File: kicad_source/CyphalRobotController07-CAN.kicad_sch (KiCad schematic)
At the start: 32 parts, among them J1 BM04B-SRSS-TB, J15 PinHeader_1x04, J16 PinHeader_1x04, J17 PinHeader_1x05, J2 RASPBERRYPI_PICO, J3 BM04B-SRSS-TB, J4 B3B-PH-SM4-TB, SW1 PTS636 SM43 SMTR LFS, U1 24LC64-I/SN, U17 SN74LVC2T45DCUR, U18 SN74LVC2T45DCUR

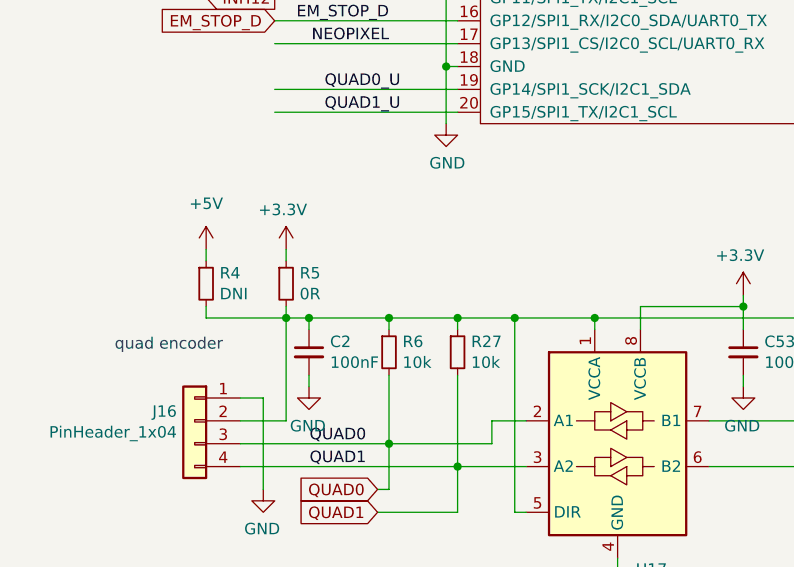
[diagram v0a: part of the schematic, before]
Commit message: finished layout near encoder level converter
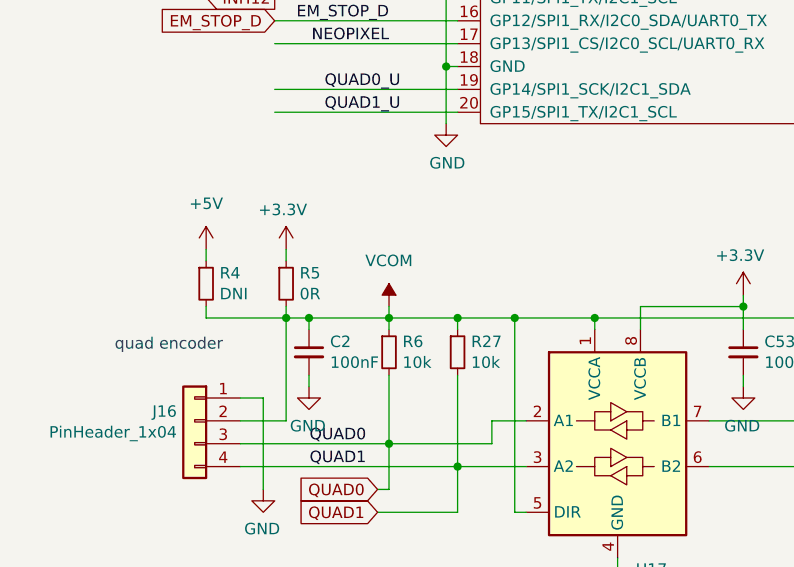
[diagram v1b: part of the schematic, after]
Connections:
- net VCOM: now reaches C2.1, C54.1, J15.2 (Pin_2), J16.2 (Pin_2), R27.1, R4.2, R5.2, R57.1, R58.1, R6.1, U17.1 (VCCA), U17.5 (DIR), U18.1 (VCCA), U18.5 (DIR)
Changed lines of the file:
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@@
+    (stroke (width 0) (type default) (color 0 0 0 0))
+  )
+  (wire (pts (xy 53.34 90.17) (xy 53.34 91.44))
     (stroke (width 0) (type default) (color 0 0 0 0))
   )
@@
     (pin "5")
   )
+  (symbol (lib_id "power:VCOM") (at 53.34 90.17 0) (unit 1)
+    (in_bom yes) (on_board yes) (fields_autoplaced)
+    (property "Reference" "#PWR?" (id 0) (at 53.34 93.98 0)
+      (effects (font (size 1.27 1.27)) hide)
+    )
+    (property "Value" "VCOM" (id 1) (at 53.34 85.09 0))
+    (property "Footprint" "" (id 2) (at 53.34 90.17 0)
+      (effects (font (size 1.27 1.27)) hide)
+    )
+    (property "Datasheet" "" (id 3) (at 53.34 90.17 0)
+      (effects (font (size 1.27 1.27)) hide)
+    )
+    (pin "1")
+  )
   (symbol (lib_id "Connector_Generic_MountingPin:Conn_01x03_MountingPin") (at 157.48 148.59 0) (mirror y) (unit 1)
     (in_bom yes) (on_board yes) (fields_autoplaced)
@@
       (reference "#PWR043") (unit 1) (value "GND") (footprint "")
     )
-    (path "/29c3546c-5738-4410-83a1-968e85712add/5bfbf133-5ed7-46d0-b93e-5a5eeb84dcff"
-      (reference "#PWR044") (unit 1) (value "+3.3V") (footprint "")
-    )
     (path "/29c3546c-5738-4410-83a1-968e85712add/09e143e1-e556-491f-aa8e-93db6198adbc"
       (reference "#PWR045") (unit 1) (value "GND") (footprint "")
@@
       (reference "#PWR047") (unit 1) (value "GND") (footprint "")
     )
-    (path "/29c3546c-5738-4410-83a1-968e85712add/900bbe2d-04d2-4af8-9360-ab393613f74d"
-      (reference "#PWR048") (unit 1) (value "+3.3V") (footprint "")
-    )
     (path "/29c3546c-5738-4410-83a1-968e85712add/00000000-0000-0000-0000-00005df4db84"
       (reference "#PWR049") (unit 1) (value "GND") (footprint "")
@@
       (reference "#PWR0171") (unit 1) (value "GND") (footprint "")
     )
+    (path "/29c3546c-5738-4410-83a1-968e85712add/34b66a16-dee4-4c29-bdba-a98382440c94"
+      (reference "#PWR?") (unit 1) (value "VCOM") (footprint "")
+    )
+    (path "/4eb5a8e0-4e6e-4b4e-8de1-2650692615d2"
+      (reference "#PWR?") (unit 1) (value "VCOM") (footprint "")
+    )
+    (path "/29c3546c-5738-4410-83a1-968e85712add/60f26f94-1bb8-4efc-8f30-f83cde330d36"
+      (reference "#PWR?") (unit 1) (value "VCOM") (footprint "")
+    )
     (path "/00000000-0000-0000-0000-000062524b56"

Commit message: used raspberry pi pico with headers
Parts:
- J2: footprint generationmake:RASPI_PICO_SOLDER_Kopie -> generationmake:RASPI_PICO_SOLDER_NO_MOUNTING
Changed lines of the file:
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@@
   (title_block
     (title "CyphalRobotController07/CAN")
-    (date "2024-01-04")
+    (date "2024-01-21")
     (rev "0.2")
     (company "generationmake")
@@
     (property "Reference" "J2" (id 0) (at 100.33 14.605 0))
     (property "Value" "RASPBERRYPI_PICO" (id 1) (at 100.33 16.9164 0))
-    (property "Footprint" "generationmake:RASPI_PICO_SOLDER_Kopie" (id 2) (at 100.33 44.45 0)
+    (property "Footprint" "generationmake:RASPI_PICO_SOLDER_NO_MOUNTING" (id 2) (at 100.33 44.45 0)
       (effects (font (size 1.27 1.27)) hide)
     )
@@
   (symbol (lib_id "power:VCOM") (at 53.34 90.17 0) (unit 1)
     (in_bom yes) (on_board yes) (fields_autoplaced)
-    (property "Reference" "#PWR?" (id 0) (at 53.34 93.98 0)
+    (property "Reference" "#PWR0172" (id 0) (at 53.34 93.98 0)
       (effects (font (size 1.27 1.27)) hide)
     )
@@
       (reference "#PWR0171") (unit 1) (value "GND") (footprint "")
     )
+    (path "/4eb5a8e0-4e6e-4b4e-8de1-2650692615d2"
+      (reference "#PWR0172") (unit 1) (value "VCOM") (footprint "")
+    )
     (path "/29c3546c-5738-4410-83a1-968e85712add/34b66a16-dee4-4c29-bdba-a98382440c94"
-      (reference "#PWR?") (unit 1) (value "VCOM") (footprint "")
-    )
-    (path "/4eb5a8e0-4e6e-4b4e-8de1-2650692615d2"
-      (reference "#PWR?") (unit 1) (value "VCOM") (footprint "")
+      (reference "#PWR0173") (unit 1) (value "VCOM") (footprint "")
     )
     (path "/29c3546c-5738-4410-83a1-968e85712add/60f26f94-1bb8-4efc-8f30-f83cde330d36"
-      (reference "#PWR?") (unit 1) (value "VCOM") (footprint "")
+      (reference "#PWR0174") (unit 1) (value "VCOM") (footprint "")
     )
     (path "/00000000-0000-0000-0000-000062524b56"
@@
     )
     (path "/00000000-0000-0000-0000-0000629e332f"
-      (reference "J2") (unit 1) (value "RASPBERRYPI_PICO") (footprint "generationmake:RASPI_PICO_SOLDER_Kopie")
+      (reference "J2") (unit 1) (value "RASPBERRYPI_PICO") (footprint "generationmake:RASPI_PICO_SOLDER_NO_MOUNTING")
     )
     (path "/00000000-0000-0000-0000-00006250779d"

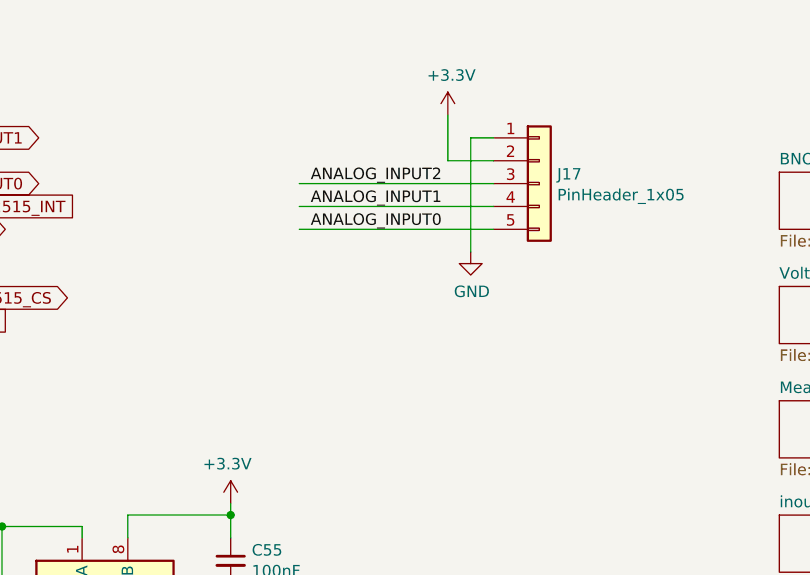
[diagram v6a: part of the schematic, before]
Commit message: connected current sense output to analog in of RP2040
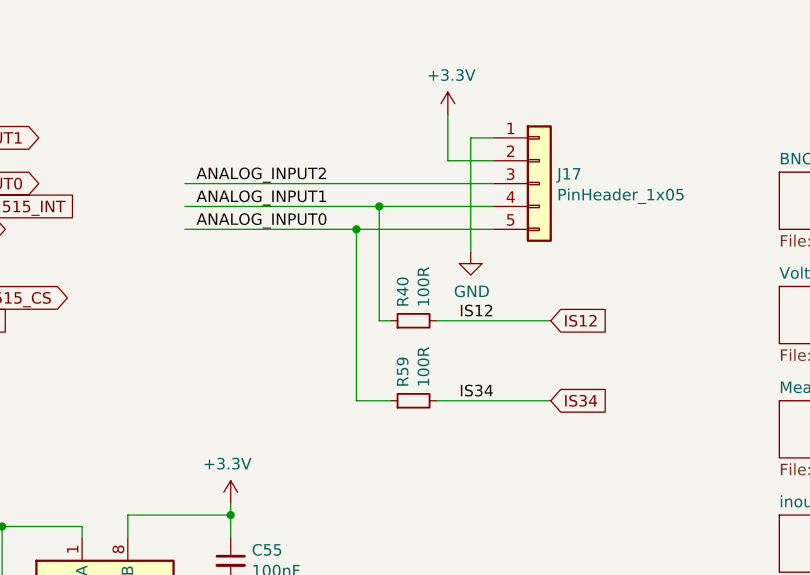
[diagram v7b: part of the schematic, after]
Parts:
- added R40, R59: 100R, Resistor_SMD:R_0603_1608Metric, symbol Device:R_Small
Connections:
- net ANALOG_INPUT0: now also R59.1
- net ANALOG_INPUT1: now also R40.1
- new net IS12: R40.2
- new net IS34: R59.2
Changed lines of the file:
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@@
   (junction (at 67.31 91.44) (diameter 0) (color 0 0 0 0)
   )
+  (junction (at 209.55 55.88) (diameter 0) (color 0 0 0 0)
+  )
   (junction (at 30.48 142.24) (diameter 0) (color 0 0 0 0)
   )
@@
   )
   (junction (at 44.45 91.44) (diameter 0) (color 0 0 0 0)
+  )
+  (junction (at 207.01 58.42) (diameter 0) (color 0 0 0 0)
   )
   (junction (at 49.53 154.94) (diameter 0) (color 0 0 0 0)
@@
     (stroke (width 0) (type default) (color 0 0 0 0))
   )
+  (wire (pts (xy 215.9 77.47) (xy 228.6 77.47))
+    (stroke (width 0) (type default) (color 0 0 0 0))
+  )
   (wire (pts (xy 114.3 148.59) (xy 111.76 148.59))
     (stroke (width 0) (type default) (color 0 0 0 0))
@@
     (stroke (width 0) (type default) (color 0 0 0 0))
   )
+  (wire (pts (xy 207.01 58.42) (xy 207.01 77.47))
+    (stroke (width 0) (type default) (color 0 0 0 0))
+  )
   (wire (pts (xy 165.1 40.64) (xy 139.7 40.64))
     (stroke (width 0) (type default) (color 0 0 0 0))
@@
     (stroke (width 0) (type default) (color 0 0 0 0))
   )
+  (wire (pts (xy 207.01 58.42) (xy 222.25 58.42))
+    (stroke (width 0) (type default) (color 0 0 0 0))
+  )
   (wire (pts (xy 168.91 148.59) (xy 168.91 144.78))
     (stroke (width 0) (type default) (color 0 0 0 0))
@@
     (stroke (width 0) (type default) (color 0 0 0 0))
   )
-  (wire (pts (xy 200.66 53.34) (xy 222.25 53.34))
-    (stroke (width 0) (type default) (color 0 0 0 0))
-  )
   (wire (pts (xy 137.16 105.41) (xy 153.67 105.41))
     (stroke (width 0) (type default) (color 0 0 0 0))
@@
     (stroke (width 0) (type default) (color 0 0 0 0))
   )
+  (wire (pts (xy 209.55 55.88) (xy 222.25 55.88))
+    (stroke (width 0) (type default) (color 0 0 0 0))
+  )
   (wire (pts (xy 165.1 105.41) (xy 165.1 102.87))
     (stroke (width 0) (type default) (color 0 0 0 0))
@@
     (stroke (width 0) (type default) (color 0 0 0 0))
   )
+  (wire (pts (xy 209.55 55.88) (xy 209.55 68.58))
+    (stroke (width 0) (type default) (color 0 0 0 0))
+  )
   (wire (pts (xy 137.16 107.95) (xy 161.29 107.95))
     (stroke (width 0) (type default) (color 0 0 0 0))
   )
-  (wire (pts (xy 200.66 58.42) (xy 222.25 58.42))
+  (wire (pts (xy 187.96 58.42) (xy 207.01 58.42))
     (stroke (width 0) (type default) (color 0 0 0 0))
   )
@@
     (stroke (width 0) (type default) (color 0 0 0 0))
   )
+  (wire (pts (xy 210.82 77.47) (xy 207.01 77.47))
+    (stroke (width 0) (type default) (color 0 0 0 0))
+  )
   (wire (pts (xy 162.56 148.59) (xy 168.91 148.59))
     (stroke (width 0) (type default) (color 0 0 0 0))
   )
-  (wire (pts (xy 200.66 55.88) (xy 222.25 55.88))
+  (wire (pts (xy 187.96 55.88) (xy 209.55 55.88))
     (stroke (width 0) (type default) (color 0 0 0 0))
   )
@@
     (stroke (width 0) (type default) (color 0 0 0 0))
   )
+  (wire (pts (xy 210.82 68.58) (xy 209.55 68.58))
+    (stroke (width 0) (type default) (color 0 0 0 0))
+  )
   (wire (pts (xy 165.1 35.56) (xy 139.7 35.56))
+    (stroke (width 0) (type default) (color 0 0 0 0))
+  )
+  (wire (pts (xy 215.9 68.58) (xy 228.6 68.58))
+    (stroke (width 0) (type default) (color 0 0 0 0))
+  )
+  (wire (pts (xy 187.96 53.34) (xy 222.25 53.34))
     (stroke (width 0) (type default) (color 0 0 0 0))
   )
@@
     (effects (font (size 1.27 1.27)) (justify right bottom))
   )
+  (label "IS12" (at 218.44 68.58 0)
+    (effects (font (size 1.27 1.27)) (justify left bottom))
+  )
   (label "MP2" (at 55.88 184.15 0)
     (effects (font (size 1.27 1.27)) (justify left bottom))
@@
     (effects (font (size 1.27 1.27)) (justify right bottom))
   )
-  (label "ANALOG_INPUT2" (at 201.93 53.34 0)
+  (label "IS34" (at 218.44 77.47 0)
+    (effects (font (size 1.27 1.27)) (justify left bottom))
+  )
+  (label "ANALOG_INPUT2" (at 189.23 53.34 0)
     (effects (font (size 1.27 1.27)) (justify left bottom))
   )
@@
     (effects (font (size 1.27 1.27)) (justify right bottom))
   )
-  (label "ANALOG_INPUT0" (at 201.93 58.42 0)
+  (label "ANALOG_INPUT0" (at 189.23 58.42 0)
     (effects (font (size 1.27 1.27)) (justify left bottom))
   )
@@
     (effects (font (size 1.27 1.27)) (justify right bottom))
   )
-  (label "ANALOG_INPUT1" (at 201.93 55.88 0)
+  (label "ANALOG_INPUT1" (at 189.23 55.88 0)
     (effects (font (size 1.27 1.27)) (justify left bottom))
   )
@@
     )
   )
+  (global_label "IS34" (shape input) (at 228.6 77.47 0) (fields_autoplaced)
+    (effects (font (size 1.27 1.27)) (justify left))
+    (property "Referenzen zwischen Schaltplänen" "${INTERSHEET_REFS}" (id 0) (at 235.1575 77.3906 0)
+      (effects (font (size 1.27 1.27)) (justify left) hide)
+    )
+  )
   (global_label "EM_STOP_D" (shape input) (at 40.64 58.42 180) (fields_autoplaced)
     (effects (font (size 1.27 1.27)) (justify right))
@@
     (property "Referenzen zwischen Schaltplänen" "${INTERSHEET_REFS}" (id 0) (at 32.9334 45.6406 0)
       (effects (font (size 1.27 1.27)) (justify right) hide)
+    )
+  )
+  (global_label "IS12" (shape input) (at 228.6 68.58 0) (fields_autoplaced)
+    (effects (font (size 1.27 1.27)) (justify left))
+    (property "Referenzen zwischen Schaltplänen" "${INTERSHEET_REFS}" (id 0) (at 235.1575 68.5006 0)
+      (effects (font (size 1.27 1.27)) (justify left) hide)
     )
   )
@@
     (pin "1")
   )
+  (symbol (lib_id "Device:R_Small") (at 213.36 68.58 90) (unit 1)
+    (in_bom yes) (on_board yes)
+    (property "Reference" "R40" (id 0) (at 212.1916 67.0814 0)
+      (effects (font (size 1.27 1.27)) (justify left))
+    )
+    (property "Value" "100R" (id 1) (at 214.503 67.0814 0)
+      (effects (font (size 1.27 1.27)) (justify left))
+    )
+    (property "Footprint" "Resistor_SMD:R_0603_1608Metric" (id 2) (at 217.17 68.58 0)
+      (effects (font (size 1.27 1.27)) hide)
+    )
+    (property "Datasheet" "~" (id 3) (at 213.36 68.58 0))
+    (pin "1")
+    (pin "2")
+  )
   (symbol (lib_id "Connector_Generic_MountingPin:Conn_01x03_MountingPin") (at 157.48 148.59 0) (mirror y) (unit 1)
     (in_bom yes) (on_board yes) (fields_autoplaced)
@@
     (property "Datasheet" "" (id 3) (at 179.07 119.38 0))
     (pin "1")
+  )
+  (symbol (lib_id "Device:R_Small") (at 213.36 77.47 90) (unit 1)
+    (in_bom yes) (on_board yes)
+    (property "Reference" "R59" (id 0) (at 212.1916 75.9714 0)
+      (effects (font (size 1.27 1.27)) (justify left))
+    )
+    (property "Value" "100R" (id 1) (at 214.503 75.9714 0)
+      (effects (font (size 1.27 1.27)) (justify left))
+    )
+    (property "Footprint" "Resistor_SMD:R_0603_1608Metric" (id 2) (at 217.17 77.47 0)
+      (effects (font (size 1.27 1.27)) hide)
+    )
+    (property "Datasheet" "~" (id 3) (at 213.36 77.47 0))
+    (pin "1")
+    (pin "2")
   )
   (symbol (lib_id "Connector_Generic:Conn_01x04") (at 31.75 102.87 0) (mirror y) (unit 1)
@@
       (reference "R39") (unit 1) (value "0R") (footprint "Resistor_SMD:R_0603_1608Metric")
     )
+    (path "/4f227162-567d-4309-8809-cb56a8c86076"
+      (reference "R40") (unit 1) (value "100R") (footprint "Resistor_SMD:R_0603_1608Metric")
+    )
     (path "/f6991e94-53cb-4fca-aa37-9cb14fb10fcb/de523bc0-a5af-4089-a2a9-c6a105520405"
       (reference "R41") (unit 1) (value "10m") (footprint "Resistor_SMD:R_1206_3216Metric")
@@
       (reference "R58") (unit 1) (value "10k") (footprint "Resistor_SMD:R_0603_1608Metric")
     )
+    (path "/729f1f15-7f90-4c42-816b-375eb7c78b88"
+      (reference "R59") (unit 1) (value "100R") (footprint "Resistor_SMD:R_0603_1608Metric")
+    )
     (path "/00000000-0000-0000-0000-000062c04ae1"

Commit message: updated 3d models
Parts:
- J1, J3: footprint Connector_JST:JST_SH_BM04B-SRSS-TB_1x04-1MP_P1.00mm_Vertical -> generationmake:JST_SH_BM04B-SRSS-TB_1x04-1MP_P1.00mm_Vertical
- J4: footprint Connector_JST:JST_PH_B3B-PH-SM4-TB_1x03-1MP_P2.00mm_Vertical -> generationmake:JST_PH_B3B-PH-SM4-TB_1x03-1MP_P2.00mm_Vertical
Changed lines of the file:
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@@
   (title_block
     (title "CyphalRobotController07/CAN")
-    (date "2024-01-21")
+    (date "2024-01-25")
     (rev "0.2")
     (company "generationmake")
@@
       (effects (font (size 1.27 1.27)) (justify left))
     )
-    (property "Footprint" "Connector_JST:JST_SH_BM04B-SRSS-TB_1x04-1MP_P1.00mm_Vertical" (id 2) (at 119.38 151.13 0)
+    (property "Footprint" "generationmake:JST_SH_BM04B-SRSS-TB_1x04-1MP_P1.00mm_Vertical" (id 2) (at 119.38 151.13 0)
       (effects (font (size 1.27 1.27)) hide)
     )
@@
       (effects (font (size 1.27 1.27)) (justify left))
     )
-    (property "Footprint" "Connector_JST:JST_SH_BM04B-SRSS-TB_1x04-1MP_P1.00mm_Vertical" (id 2) (at 53.34 172.72 0)
+    (property "Footprint" "generationmake:JST_SH_BM04B-SRSS-TB_1x04-1MP_P1.00mm_Vertical" (id 2) (at 53.34 172.72 0)
       (effects (font (size 1.27 1.27)) hide)
     )
@@
     (property "Reference" "J4" (id 0) (at 157.48 139.7 0))
     (property "Value" "B3B-PH-SM4-TB" (id 1) (at 157.48 142.24 0))
-    (property "Footprint" "Connector_JST:JST_PH_B3B-PH-SM4-TB_1x03-1MP_P2.00mm_Vertical" (id 2) (at 157.48 148.59 0)
+    (property "Footprint" "generationmake:JST_PH_B3B-PH-SM4-TB_1x03-1MP_P2.00mm_Vertical" (id 2) (at 157.48 148.59 0)
       (effects (font (size 1.27 1.27)) hide)
     )
@@
     )
     (path "/00000000-0000-0000-0000-00006250ded9"
-      (reference "J1") (unit 1) (value "BM04B-SRSS-TB") (footprint "Connector_JST:JST_SH_BM04B-SRSS-TB_1x04-1MP_P1.00mm_Vertical")
+      (reference "J1") (unit 1) (value "BM04B-SRSS-TB") (footprint "generationmake:JST_SH_BM04B-SRSS-TB_1x04-1MP_P1.00mm_Vertical")
     )
     (path "/00000000-0000-0000-0000-0000629e332f"
@@
     )
     (path "/00000000-0000-0000-0000-00006250779d"
-      (reference "J3") (unit 1) (value "BM04B-SRSS-TB") (footprint "Connector_JST:JST_SH_BM04B-SRSS-TB_1x04-1MP_P1.00mm_Vertical")
+      (reference "J3") (unit 1) (value "BM04B-SRSS-TB") (footprint "generationmake:JST_SH_BM04B-SRSS-TB_1x04-1MP_P1.00mm_Vertical")
     )
     (path "/551049a7-4d09-455c-ac39-872acb209e74"
-      (reference "J4") (unit 1) (value "B3B-PH-SM4-TB") (footprint "Connector_JST:JST_PH_B3B-PH-SM4-TB_1x03-1MP_P2.00mm_Vertical")
+      (reference "J4") (unit 1) (value "B3B-PH-SM4-TB") (footprint "generationmake:JST_PH_B3B-PH-SM4-TB_1x03-1MP_P2.00mm_Vertical")
     )
     (path "/00000000-0000-0000-0000-00005ed92f9c/00000000-0000-0000-0000-000062500ca8"
